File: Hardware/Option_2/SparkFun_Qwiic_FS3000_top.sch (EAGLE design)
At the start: 29 parts, among them J2 QWIIC_RA, J3 QWIIC_RA, U1 FS3000

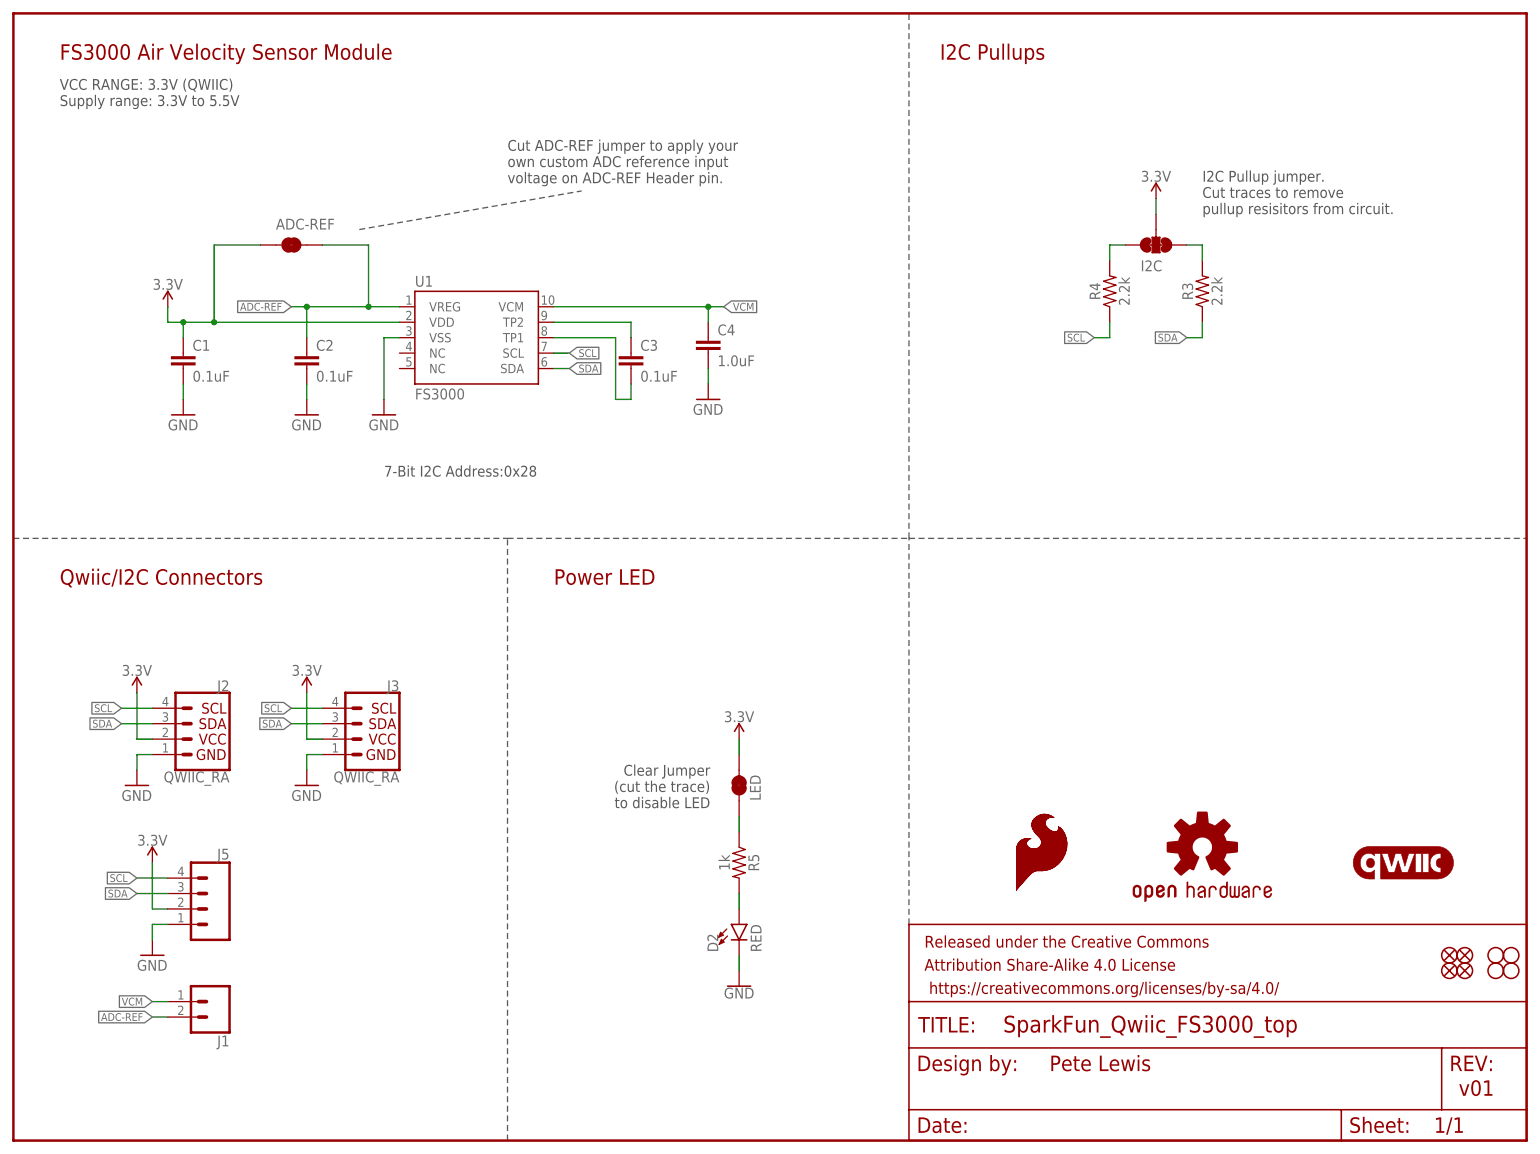
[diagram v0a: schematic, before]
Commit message: Group Review Changes
-Buzzard labels on VCM/ADCR changed to be correct inputs/outputs end type
-Added in solder pads for two versions (7.23m/s vs 15m/s) (1005/1015)
-Moved"supply range" to below the IC and change to "VDD range".
-schematic cleanup - power LED jumper paragraph. space in I2C address.
-added space between "I2C address" and "0x28" in board silk
-added name/flame logo to board silk.
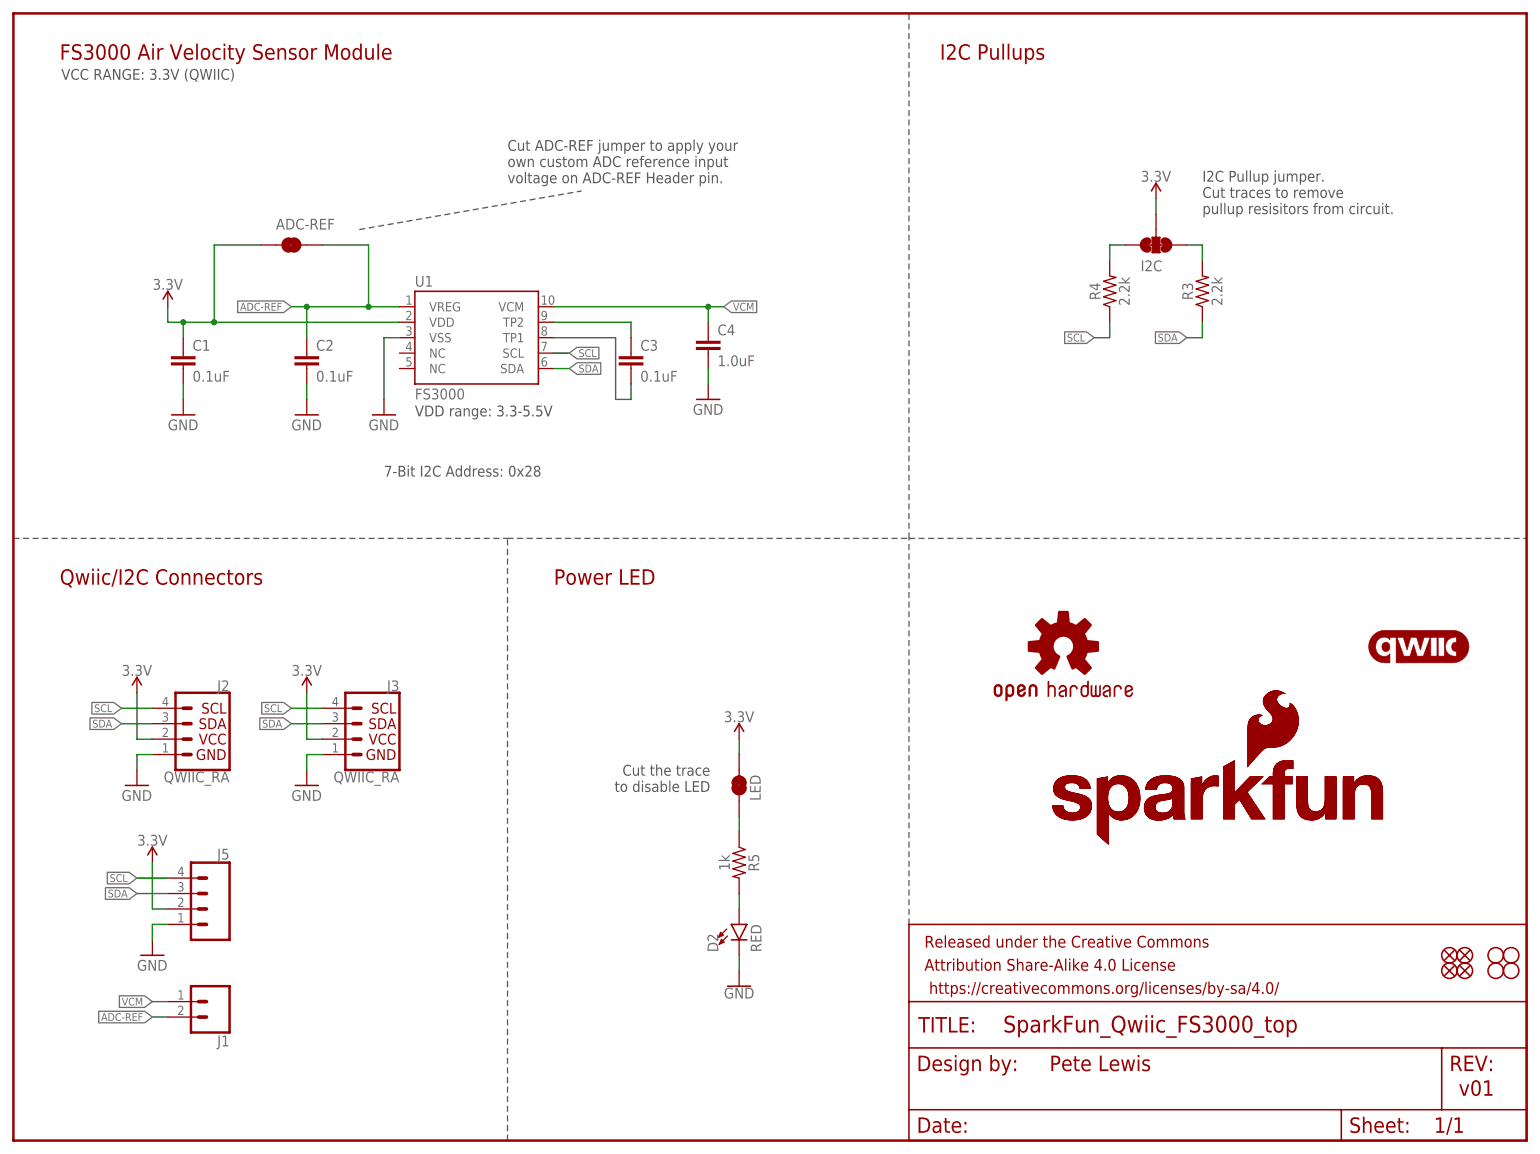
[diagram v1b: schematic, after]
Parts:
- removed LOGO2: SFE_LOGO_FLAME.1_INCH, SparkFun-Aesthetics:SFE_LOGO_FLAME.1_INCH
- added LOGO5: SFE_LOGO_NAME_FLAME.1_INCH, SparkFun-Aesthetics:SFE_LOGO_NAME_FLAME.1_INCH
- LOGO3: value SFE_LOGO_FLAME.1_INCH -> SFE_LOGO_NAME_FLAME.1_INCH; device SparkFun-Aesthetics:SFE_LOGO_FLAME.1_INCH -> SparkFun-Aesthetics:SFE_LOGO_NAME_FLAME.1_INCH
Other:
- note added: "7-Bit I2C Address: 0x28"
- note added: "Cut the trace to disable LED"
- note added: "VCC RANGE: 3.3V (QWIIC)"
- note added: "VDD range: 3.3-5.5V"
- note removed: "7-Bit I2C Address:0x28"
- note removed: "Clear Jumper (cut the trace) to disable LED"
- note removed: "VCC RANGE: 3.3V (QWIIC) Supply range: 3.3V to 5.5V"
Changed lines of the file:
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@@
 <part name="GND13" library="SparkFun-PowerSymbols" library_urn="urn:adsk.eagle:library:530" deviceset="GND" device=""/>
 <part name="JP1" library="SparkFun-Jumpers" deviceset="JUMPER-SMT_2_NC_TRACE" device="_SILK" package3d_urn="urn:adsk.eagle:package:39281/1" value="LED"/>
-<part name="LOGO3" library="SparkFun-Aesthetics" deviceset="SFE_LOGO_FLAME" device=".1_INCH"/>
 <part name="SUPPLY12" library="SparkFun-PowerSymbols" deviceset="3.3V" device=""/>
 <part name="C2" library="SparkFun-Capacitors" deviceset="0.1UF" device="-0402T-16V-10%" value="0.1uF"/>
@@
 <part name="GND3" library="SparkFun" deviceset="GND" device=""/>
 <part name="ADC-REF" library="SparkFun-Jumpers" deviceset="JUMPER-SMT_2_NC_TRACE" device="_SILK" package3d_urn="urn:adsk.eagle:package:39281/1" value=""/>
-<part name="LOGO2" library="SparkFun-Aesthetics" deviceset="SFE_LOGO_FLAME" device=".1_INCH"/>
 <part name="JP4" library="SparkFun" deviceset="STAND-OFF" device=""/>
 <part name="JP7" library="SparkFun" deviceset="STAND-OFF" device=""/>
@@
 <part name="J3" library="SparkFun-Connectors" deviceset="QWIIC_CONNECTOR" device="JS-1MM" value="QWIIC_RA"/>
 <part name="GND5" library="SparkFun" deviceset="GND" device=""/>
+<part name="LOGO5" library="SparkFun-Aesthetics" deviceset="SFE_LOGO_NAME_FLAME" device=".1_INCH"/>
+<part name="LOGO3" library="SparkFun-Aesthetics" deviceset="SFE_LOGO_NAME_FLAME" device=".1_INCH"/>
 </parts>
 <sheets>
 <sheet>
 <plain>
-<text x="60.96" y="109.22" size="1.778" layer="97" font="vector">7-Bit I2C Address:0x28</text>
+<text x="60.96" y="109.22" size="1.778" layer="97" font="vector">7-Bit I2C Address: 0x28</text>
 <text x="170.434" y="11.43" size="2.54" layer="94" font="vector">Pete Lewis</text>
 <text x="237.744" y="7.366" size="2.54" layer="94" font="vector">v01</text>
@@
 Cut traces to remove
 pullup resisitors from circuit.</text>
-<text x="114.6302" y="61.7982" size="1.778" layer="97" font="vector" rot="R180">Clear Jumper
-(cut the trace)
+<text x="114.6302" y="61.7982" size="1.778" layer="97" font="vector" rot="R180">Cut the trace
 to disable LED</text>
 <text x="88.9" y="91.44" size="2.54" layer="94" font="vector">Power LED</text>
@@
 <wire x1="81.28" y1="0" x2="81.28" y2="99.06" width="0.1524" layer="97" style="longdash"/>
 <wire x1="147.32" y1="35.56" x2="147.32" y2="99.06" width="0.1524" layer="97" style="longdash"/>
-<text x="7.62" y="170.18" size="1.778" layer="97" font="vector">VCC RANGE: 3.3V (QWIIC)
-Supply range: 3.3V to 5.5V</text>
+<text x="7.874" y="174.498" size="1.778" layer="97" font="vector">VCC RANGE: 3.3V (QWIIC)</text>
 <wire x1="147.32" y1="99.06" x2="147.32" y2="185.42" width="0.1524" layer="97" style="longdash"/>
 <text x="152.4" y="177.8" size="2.54" layer="94" font="vector">I2C Pullups</text>
@@
 voltage on ADC-REF Header pin.</text>
 <wire x1="56.896" y1="149.86" x2="93.472" y2="156.21" width="0.2032" layer="97" style="shortdash"/>
+<text x="66.04" y="119.126" size="1.778" layer="97" font="vector">VDD range: 3.3-5.5V</text>
 </plain>
 <instances>
@@
 <attribute name="VALUE" x="29.464" y="124.841" size="1.778" layer="96" font="vector"/>
 </instance>
-<instance part="LOGO1" gate="G$1" x="195.58" y="48.26" smashed="yes"/>
+<instance part="LOGO1" gate="G$1" x="172.72" y="81.28" smashed="yes"/>
 <instance part="JP11" gate="G$1" x="238.76" y="27.94" smashed="yes"/>
 <instance part="JP5" gate="G$1" x="238.76" y="30.48" smashed="yes"/>
@@
 <attribute name="NAME" x="35.56" y="46.228" size="1.778" layer="95" font="vector" rot="MR0"/>
 </instance>
-<instance part="LOGO4" gate="G$1" x="228.6" y="45.72" smashed="yes"/>
+<instance part="LOGO4" gate="G$1" x="231.14" y="81.28" smashed="yes"/>
 <instance part="JP8" gate="G$1" x="243.84" y="30.48" smashed="yes"/>
 <instance part="D2" gate="G$1" x="119.38" y="35.56" smashed="yes">
@@
 <attribute name="VALUE" x="121.158" y="55.88" size="1.778" layer="96" font="vector" rot="R90" align="top-left"/>
 </instance>
-<instance part="LOGO3" gate="G$1" x="164.5666" y="40.5384" smashed="yes"/>
 <instance part="SUPPLY12" gate="G$1" x="25.4" y="137.16" smashed="yes">
 <attribute name="VALUE" x="25.4" y="139.954" size="1.778" layer="96" font="vector" align="bottom-center"/>
@@
 <attribute name="VALUE" x="43.18" y="144.78" size="1.778" layer="96" font="vector" align="top-left"/>
 </instance>
-<instance part="LOGO2" gate="G$1" x="164.5666" y="40.5384" smashed="yes"/>
 <instance part="JP4" gate="G$1" x="246.38" y="27.94" smashed="yes"/>
 <instance part="JP7" gate="G$1" x="243.84" y="27.94" smashed="yes"/>
@@
 <attribute name="VALUE" x="45.72" y="55.88" size="1.778" layer="96" font="vector"/>
 </instance>
+<instance part="LOGO5" gate="G$1" x="170.18" y="48.26" smashed="yes"/>
+<instance part="LOGO3" gate="G$1" x="170.18" y="48.26" smashed="yes"/>
 </instances>
 <busses>
